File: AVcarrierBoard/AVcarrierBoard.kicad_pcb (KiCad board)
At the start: 4 copper layers, 253.6 x 59 mm, 18 parts, among them J1 Mech_Switch, J2 Mech_Switch, J3 MainRecov, J4 DrogRecov, J5 Staging, J6 Mech_Switch, U2 WiFi Switch, U3 EggtimerQuantum, U4 EggfinderMini/FeatherGPS, U5 Blue_Raven

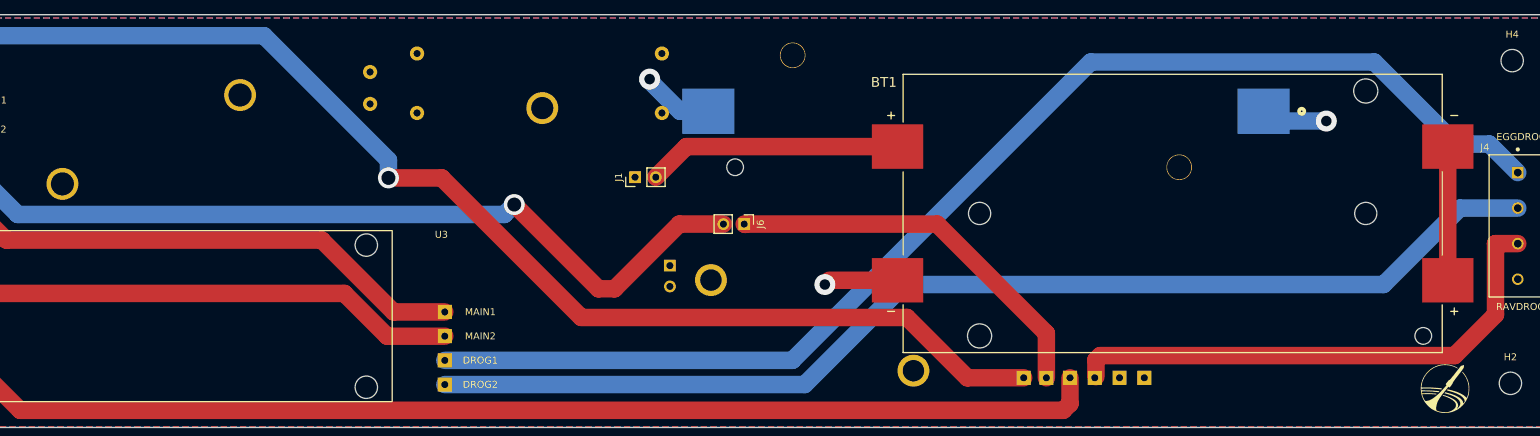
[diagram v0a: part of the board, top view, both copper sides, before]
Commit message: Solved DRC
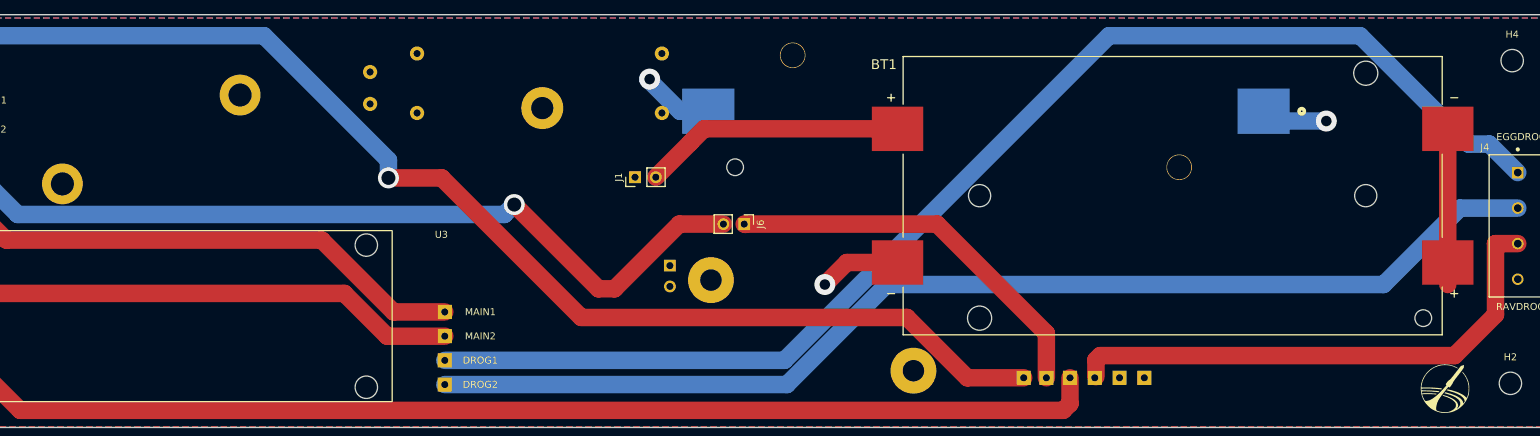
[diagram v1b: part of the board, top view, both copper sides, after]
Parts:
- moved BT1 2.54 mm to (221.3, 91.4)
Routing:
- net DROG1: track 177.6 -> 180.7 mm
- net +7.5V: track 36.4 -> 37.4 mm
- net GND: track 10.6 -> 11.7 mm
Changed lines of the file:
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@@
   )
   (footprint "COTS_Boards:BAT_1048P" (layer "F.Cu")
-    (at 221.32 93.98)
+    (at 221.32 91.44)
     (property "Sheetfile" "AVcarrierBoard.kicad_sch")
     (property "Sheetname" "")
@@
         (effects (font (size 1 1) (thickness 0.15)) (justify mirror))
     )
-    (fp_text user "3rd" (at 51.5 -7.62 -90 unlocked) (layer "B.SilkS")
+    (fp_text user "+" (at 65.5 -7.62 -90 unlocked) (layer "B.SilkS")
+        (effects (font (size 1 1) (thickness 0.15)) (justify mirror))
+    )
+    (fp_text user "Gnd" (at 61.96 -7.62 -90 unlocked) (layer "B.SilkS")
+        (effects (font (size 1 1) (thickness 0.15)) (justify mirror))
+    )
+    (fp_text user "Main" (at 54.88 -7.62 -90 unlocked) (layer "B.SilkS")
+        (effects (font (size 1 1) (thickness 0.15)) (justify mirror))
+    )
+    (fp_text user "4th" (at 48.26 -7.62 270 unlocked) (layer "B.SilkS")
         (effects (font (size 1 1) (thickness 0.15)) (justify mirror))
     )
@@
         (effects (font (size 1 1) (thickness 0.15)) (justify mirror))
     )
-    (fp_text user "4th" (at 48.26 -7.62 270 unlocked) (layer "B.SilkS")
-        (effects (font (size 1 1) (thickness 0.15)) (justify mirror))
-    )
-    (fp_text user "Main" (at 54.88 -7.62 -90 unlocked) (layer "B.SilkS")
-        (effects (font (size 1 1) (thickness 0.15)) (justify mirror))
-    )
-    (fp_text user "Gnd" (at 61.96 -7.62 -90 unlocked) (layer "B.SilkS")
-        (effects (font (size 1 1) (thickness 0.15)) (justify mirror))
-    )
-    (fp_text user "+" (at 65.5 -7.62 -90 unlocked) (layer "B.SilkS")
+    (fp_text user "3rd" (at 51.5 -7.62 -90 unlocked) (layer "B.SilkS")
         (effects (font (size 1 1) (thickness 0.15)) (justify mirror))
     )
@@
     (fp_rect (start 0 2.54) (end 68.58 -22.86)
       (stroke (width 0.05) (type default)) (fill none) (layer "B.CrtYd"))
-    (pad "" np_thru_hole circle (at 3.556 -16.51) (size 4.56 4.56) (drill 3.06832) (layers "F&B.Cu" "*.Mask"))
-    (pad "" np_thru_hole circle (at 32.4993 -3.556) (size 4.56 4.56) (drill 3.06832) (layers "F&B.Cu" "*.Mask"))
+    (pad "" np_thru_hole circle (at 3.556 -16.51) (size 6.56082 6.56082) (drill 3.06832) (layers "*.Cu" "*.Mask"))
+    (pad "" np_thru_hole circle (at 32.4993 -3.556) (size 6.56082 6.56082) (drill 3.06832) (layers "*.Cu" "*.Mask"))
     (pad "1" thru_hole rect (at 65.5 -2.54 90) (size 2.032 2.032) (drill 1) (layers "*.Cu" "*.Mask")
       (net 11 "WIFI_PWR_1S") (pinfunction "+") (pintype "input"))
@@
     (fp_rect (start -2 2) (end 49.08 -22)
       (stroke (width 0.05) (type default)) (fill none) (layer "B.CrtYd"))
-    (pad "" np_thru_hole circle (at 3.302 -3.81) (size 4.56 4.56) (drill 3.302) (layers "F&B.Cu" "*.Mask"))
-    (pad "" np_thru_hole circle (at 28.702 -16.51) (size 4.56 4.56) (drill 3.302) (layers "F&B.Cu" "*.Mask"))
+    (pad "" np_thru_hole circle (at 3.302 -3.81) (size 5.842 5.842) (drill 3.302) (layers "*.Cu" "*.Mask"))
+    (pad "" np_thru_hole circle (at 28.702 -16.51) (size 5.842 5.842) (drill 3.302) (layers "*.Cu" "*.Mask"))
     (pad "1" thru_hole circle (at 47.284587 -15.24) (size 2.032 2.032) (drill 1) (layers "*.Cu" "*.Mask")
       (net 16 "PWR_2S") (pinfunction "VDD") (pintype "power_in"))
@@
         (effects (font (size 1 1) (thickness 0.15)) (justify mirror))
     )
+    (fp_text user "BATT" (at 19.66 5.81 180 unlocked) (layer "B.SilkS")
+        (effects (font (size 1 1) (thickness 0.1)) (justify left bottom mirror))
+    )
     (fp_text user "OUT" (at -6 5 180 unlocked) (layer "B.SilkS")
         (effects (font (size 1 1) (thickness 0.1)) (justify left bottom mirror))
     )
+    (fp_text user "-" (at 23 10.5 180 unlocked) (layer "B.SilkS")
+        (effects (font (size 1 1) (thickness 0.15)) (justify mirror))
+    )
     (fp_text user "+" (at 23 2 180 unlocked) (layer "B.SilkS")
         (effects (font (size 1 1) (thickness 0.15)) (justify mirror))
@@
         (effects (font (size 1 1) (thickness 0.15)) (justify mirror))
     )
-    (fp_text user "-" (at 23 10.5 180 unlocked) (layer "B.SilkS")
-        (effects (font (size 1 1) (thickness 0.15)) (justify mirror))
-    )
     (fp_text user "+" (at -4 2 180 unlocked) (layer "B.SilkS")
         (effects (font (size 1 1) (thickness 0.15)) (justify mirror))
-    )
-    (fp_text user "BATT" (at 19.66 5.81 180 unlocked) (layer "B.SilkS")
-        (effects (font (size 1 1) (thickness 0.1)) (justify left bottom mirror))
     )
     (fp_text user "${REFERENCE}" (at 0 -2.5 180 unlocked) (layer "B.Fab")
@@
     (fp_rect (start 0 38) (end 19 0)
       (stroke (width 0.1) (type default)) (fill none) (layer "B.Fab"))
-    (pad "" np_thru_hole circle (at 9.9 9.8) (size 4.56 4.56) (drill 3.18) (layers "F&B.Cu" "*.Mask"))
+    (pad "" np_thru_hole circle (at 9.9 9.8) (size 6 6) (drill 3.18) (layers "*.Cu" "*.Mask"))
     (pad "1" thru_hole circle (at 27 2) (size 2.032 2.032) (drill 1) (layers "*.Cu" "*.Mask")
       (net 7 "COTSWIFI+") (pinfunction "Batt+") (pintype "power_in"))
@@
   )
   (via (at 243.2812 80.772) (size 3) (drill 1.5) (layers "F.Cu" "B.Cu") (free) (net 1))
+  (segment (start 243.2812 80.772) (end 219.9132 104.14) (width 2.5) (layer "In1.Cu") (net 1))
+  (segment (start 219.9132 104.14) (end 180.34 104.14) (width 2.5) (layer "In1.Cu") (net 1))
+  (segment (start 180.34 104.14) (end 171.958 112.522) (width 2.5) (layer "In1.Cu") (net 1))
+  (segment (start 155.4988 112.522) (end 149.4536 106.4768) (width 2.5) (layer "In1.Cu") (net 1))
   (segment (start 149.4536 106.4768) (end 149.4536 104.4126) (width 2.5) (layer "In1.Cu") (net 1))
-  (segment (start 217.3732 106.68) (end 177.8 106.68) (width 2.5) (layer "In1.Cu") (net 1))
-  (segment (start 243.2812 80.772) (end 217.3732 106.68) (width 2.5) (layer "In1.Cu") (net 1))
   (segment (start 171.958 112.522) (end 155.4988 112.522) (width 2.5) (layer "In1.Cu") (net 1))
-  (segment (start 155.4988 112.522) (end 149.4536 106.4768) (width 2.5) (layer "In1.Cu") (net 1))
-  (segment (start 177.8 106.68) (end 171.958 112.522) (width 2.5) (layer "In1.Cu") (net 1))
   (segment (start 235.712 80.772) (end 234.315 79.375) (width 2.5) (layer "B.Cu") (net 1))
   (segment (start 243.2812 80.772) (end 235.712 80.772) (width 2.5) (layer "B.Cu") (net 1))
-  (segment (start 181.99 103.535) (end 172.2074 103.535) (width 2.5) (layer "F.Cu") (net 2))
+  (segment (start 174.7474 100.995) (end 181.99 100.995) (width 2.5) (layer "F.Cu") (net 2))
+  (segment (start 172.2074 103.535) (end 174.7474 100.995) (width 2.5) (layer "F.Cu") (net 2))
   (segment (start 172.2074 103.535) (end 171.6024 104.14) (width 0.25) (layer "F.Cu") (net 2))
   (via (at 171.6024 104.14) (size 3) (drill 1.5) (layers "F.Cu" "B.Cu") (net 2))
@@
   (segment (start 155.3972 78.2072) (end 155.3972 90.5256) (width 2.5) (layer "In1.Cu") (net 7))
   (segment (start 149.4536 96.4692) (end 149.4536 101.4426) (width 2.5) (layer "In1.Cu") (net 7))
-  (segment (start 151.8136 84.425) (end 181.99 84.425) (width 2.5) (layer "F.Cu") (net 8))
-  (segment (start 147.4402 88.7984) (end 151.8136 84.425) (width 2.5) (layer "F.Cu") (net 8))
+  (segment (start 147.4402 88.7984) (end 152.4 83.8386) (width 2.5) (layer "F.Cu") (net 8))
+  (segment (start 152.4 83.82) (end 154.335 81.885) (width 2.5) (layer "F.Cu") (net 8))
+  (segment (start 152.4 83.8386) (end 152.4 83.82) (width 2.5) (layer "F.Cu") (net 8))
+  (segment (start 154.335 81.885) (end 181.99 81.885) (width 2.5) (layer "F.Cu") (net 8))
+  (segment (start 248.125839 68.58) (end 212.217151 68.58) (width 2.5) (layer "B.Cu") (net 9))
   (segment (start 270.65 88.1375) (end 266.576 84.0635) (width 2.5) (layer "B.Cu") (net 9))
-  (segment (start 166.96 114.98) (end 117.275 114.98) (width 2.5) (layer "B.Cu") (net 9))
-  (segment (start 250.1392 72.3392) (end 209.6008 72.3392) (width 2.5) (layer "B.Cu") (net 9))
-  (segment (start 266.576 84.0635) (end 261.8635 84.0635) (width 2.5) (layer "B.Cu") (net 9))
-  (segment (start 209.6008 72.3392) (end 166.96 114.98) (width 2.5) (layer "B.Cu") (net 9))
-  (segment (start 261.8635 84.0635) (end 250.1392 72.3392) (width 2.5) (layer "B.Cu") (net 9))
-  (segment (start 183.015527 104.14) (end 168.715527 118.44) (width 2.5) (layer "B.Cu") (net 10))
+  (segment (start 165.817151 114.98) (end 117.275 114.98) (width 2.5) (layer "B.Cu") (net 9))
+  (segment (start 266.576 84.0635) (end 263.609339 84.0635) (width 2.5) (layer "B.Cu") (net 9))
+  (segment (start 263.609339 84.0635) (end 248.125839 68.58) (width 2.5) (layer "B.Cu") (net 9))
+  (segment (start 212.217151 68.58) (end 165.817151 114.98) (width 2.5) (layer "B.Cu") (net 9))
+  (segment (start 166.175527 118.44) (end 117.275 118.44) (width 2.5) (layer "B.Cu") (net 10))
+  (segment (start 180.475527 104.14) (end 166.175527 118.44) (width 2.5) (layer "B.Cu") (net 10))
   (segment (start 262.3825 93.2175) (end 251.46 104.14) (width 2.5) (layer "B.Cu") (net 10))
-  (segment (start 251.46 104.14) (end 183.015527 104.14) (width 2.5) (layer "B.Cu") (net 10))
-  (segment (start 168.715527 118.44) (end 117.275 118.44) (width 2.5) (layer "B.Cu") (net 10))
   (segment (start 270.65 93.2175) (end 262.3825 93.2175) (width 2.5) (layer "B.Cu") (net 10))
+  (segment (start 251.46 104.14) (end 180.475527 104.14) (width 2.5) (layer "B.Cu") (net 10))
   (segment (start 160.2308 95.504) (end 160.2308 95.5548) (width 2.5) (layer "F.Cu") (net 12))
   (segment (start 187.647386 95.504) (end 160.0708 95.504) (width 2.5) (layer "F.Cu") (net 12))

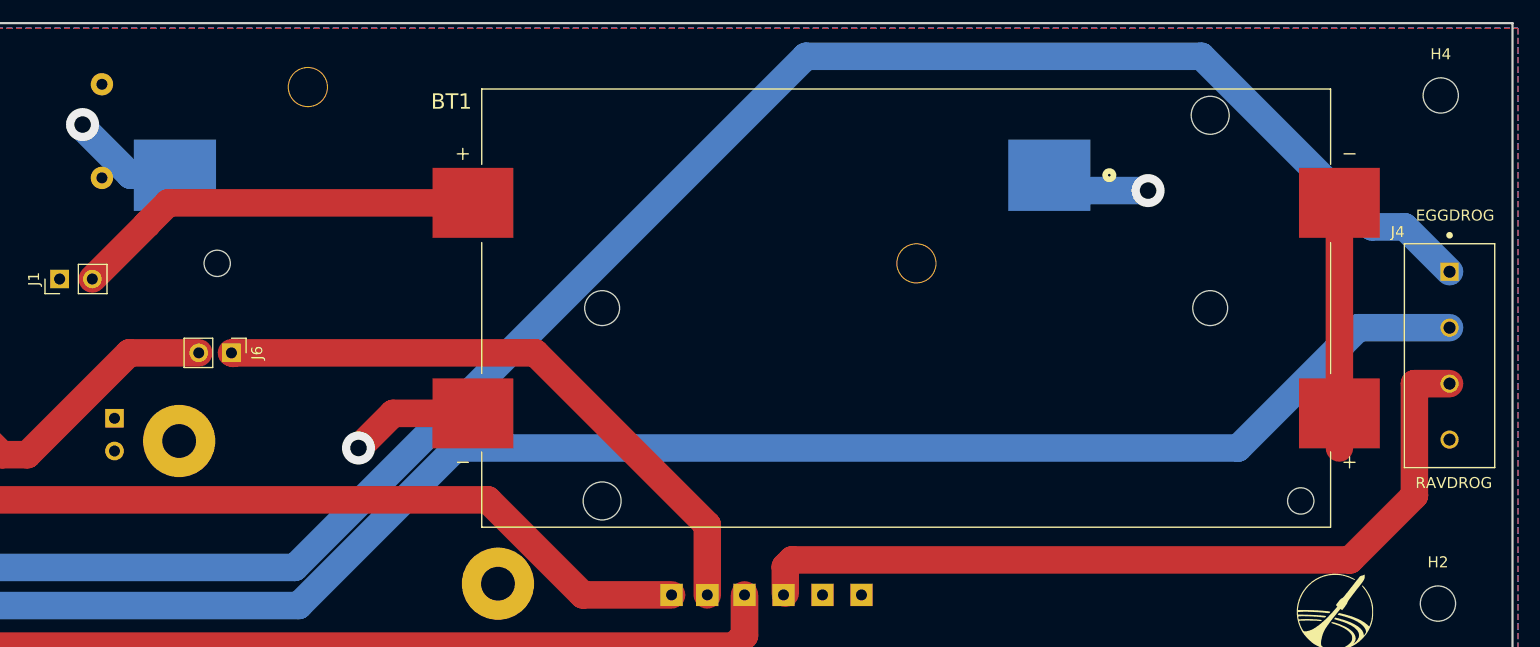
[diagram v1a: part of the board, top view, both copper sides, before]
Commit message: Changed location of 1S battery and remade STEP
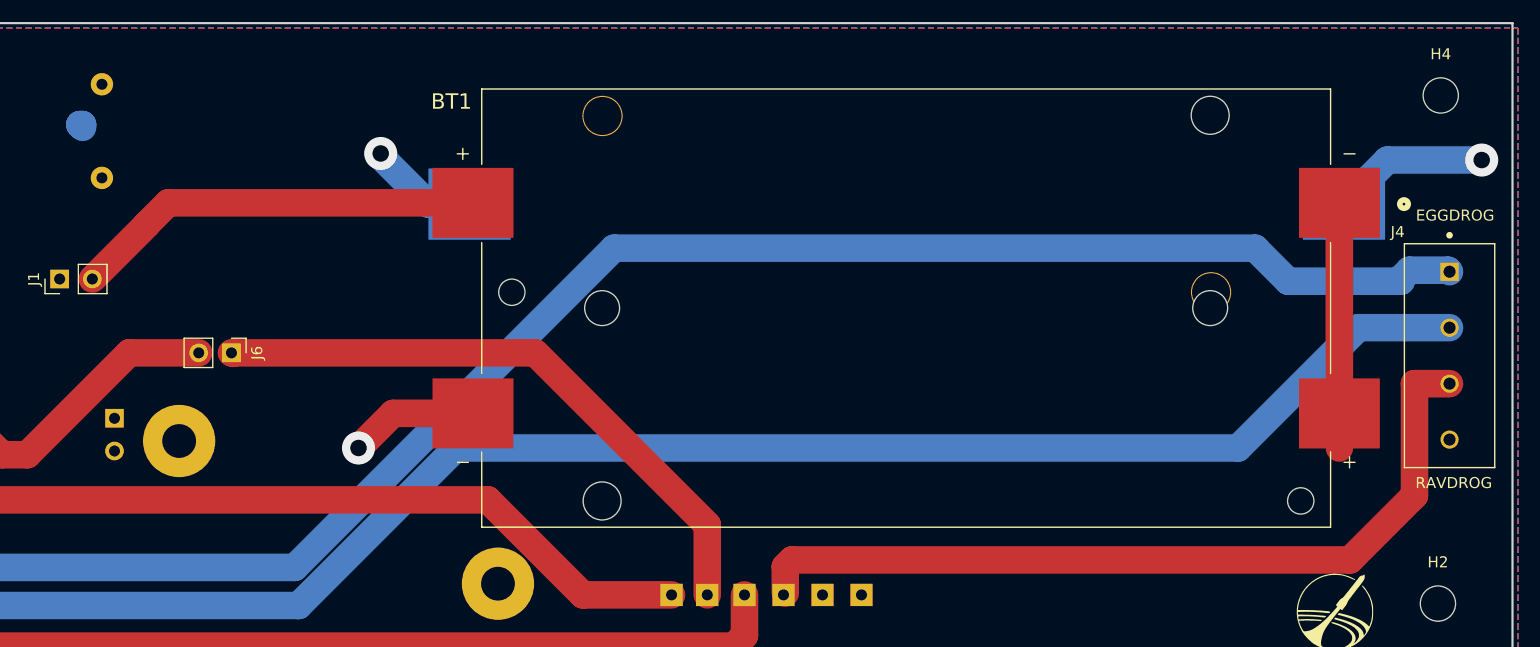
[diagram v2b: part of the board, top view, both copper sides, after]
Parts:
- moved BT2 26.9 mm to (221.4, 82.0)
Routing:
- net +3V8: track 121.1 -> 157.2 mm
- net DROG1: track 180.7 -> 167.2 mm
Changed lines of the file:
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@@
   )
   (footprint "COTS_Boards:1042P_KEY" (layer "B.Cu")
-    (at 194.6275 79.375 180)
+    (at 221.3775 81.999 180)
     (tags "1042P ")
     (property "Sheetfile" "AVcarrierBoard.kicad_sch")
@@
     (effects (font (size 1 1) (thickness 0.15)) (justify right bottom))
   )
-  (via (at 243.2812 80.772) (size 3) (drill 1.5) (layers "F.Cu" "B.Cu") (free) (net 1))
+  (via (at 273.5692 78) (size 3) (drill 1.5) (layers "F.Cu" "B.Cu") (free) (net 1))
+  (segment (start 251.228 80.772) (end 254 78) (width 2.5) (layer "In1.Cu") (net 1))
   (segment (start 243.2812 80.772) (end 219.9132 104.14) (width 2.5) (layer "In1.Cu") (net 1))
+  (segment (start 254 78) (end 273.5692 78) (width 2.5) (layer "In1.Cu") (net 1))
+  (segment (start 243.2812 80.772) (end 251.228 80.772) (width 2.5) (layer "In1.Cu") (net 1))
   (segment (start 219.9132 104.14) (end 180.34 104.14) (width 2.5) (layer "In1.Cu") (net 1))
   (segment (start 180.34 104.14) (end 171.958 112.522) (width 2.5) (layer "In1.Cu") (net 1))
@@
   (segment (start 149.4536 106.4768) (end 149.4536 104.4126) (width 2.5) (layer "In1.Cu") (net 1))
   (segment (start 171.958 112.522) (end 155.4988 112.522) (width 2.5) (layer "In1.Cu") (net 1))
-  (segment (start 235.712 80.772) (end 234.315 79.375) (width 2.5) (layer "B.Cu") (net 1))
-  (segment (start 243.2812 80.772) (end 235.712 80.772) (width 2.5) (layer "B.Cu") (net 1))
+  (segment (start 265 78) (end 273.5692 78) (width 2.5) (layer "B.Cu") (net 1))
+  (segment (start 261.065 81.999) (end 261.065 81.935) (width 0.25) (layer "B.Cu") (net 1))
+  (segment (start 273.5682 78) (end 273.5692 78.001) (width 2.5) (layer "B.Cu") (net 1))
+  (segment (start 261.065 81.935) (end 265 78) (width 2.5) (layer "B.Cu") (net 1))
   (segment (start 174.7474 100.995) (end 181.99 100.995) (width 2.5) (layer "F.Cu") (net 2))
   (segment (start 172.2074 103.535) (end 174.7474 100.995) (width 2.5) (layer "F.Cu") (net 2))
@@
   (segment (start 152.4 83.8386) (end 152.4 83.82) (width 2.5) (layer "F.Cu") (net 8))
   (segment (start 154.335 81.885) (end 181.99 81.885) (width 2.5) (layer "F.Cu") (net 8))
-  (segment (start 248.125839 68.58) (end 212.217151 68.58) (width 2.5) (layer "B.Cu") (net 9))
-  (segment (start 270.65 88.1375) (end 266.576 84.0635) (width 2.5) (layer "B.Cu") (net 9))
+  (segment (start 270.5125 88) (end 267 88) (width 2.5) (layer "B.Cu") (net 9))
+  (segment (start 194.797151 86) (end 165.817151 114.98) (width 2.5) (layer "B.Cu") (net 9))
+  (segment (start 267 88) (end 266.2488 88.7512) (width 2.5) (layer "B.Cu") (net 9))
+  (segment (start 270.65 88.1375) (end 270.5125 88) (width 2.5) (layer "B.Cu") (net 9))
+  (segment (start 266.2488 88.7512) (end 266.2488 89) (width 2.5) (layer "B.Cu") (net 9))
   (segment (start 165.817151 114.98) (end 117.275 114.98) (width 2.5) (layer "B.Cu") (net 9))
-  (segment (start 266.576 84.0635) (end 263.609339 84.0635) (width 2.5) (layer "B.Cu") (net 9))
-  (segment (start 263.609339 84.0635) (end 248.125839 68.58) (width 2.5) (layer "B.Cu") (net 9))
-  (segment (start 212.217151 68.58) (end 165.817151 114.98) (width 2.5) (layer "B.Cu") (net 9))
+  (segment (start 266.2488 89) (end 256 89) (width 2.5) (layer "B.Cu") (net 9))
+  (segment (start 256 89) (end 253 86) (width 2.5) (layer "B.Cu") (net 9))
+  (segment (start 253 86) (end 194.797151 86) (width 2.5) (layer "B.Cu") (net 9))
   (segment (start 166.175527 118.44) (end 117.275 118.44) (width 2.5) (layer "B.Cu") (net 10))
   (segment (start 180.475527 104.14) (end 166.175527 118.44) (width 2.5) (layer "B.Cu") (net 10))
@@
   (segment (start 267.4625 98.2975) (end 267.4625 108.4575) (width 2.5) (layer "F.Cu") (net 13))
   (segment (start 270.65 98.2975) (end 267.4625 98.2975) (width 2.5) (layer "F.Cu") (net 13))
-  (via (at 146.558 74.7776) (size 3) (drill 1.5) (layers "F.Cu" "B.Cu") (net 14))
+  (via (at 173.618 77.4026) (size 3) (drill 1.5) (layers "F.Cu" "B.Cu") (net 14))
   (segment (start 146.558 74.7776) (end 146.304 74.7776) (width 2.5) (layer "B.Cu") (net 14))
-  (segment (start 154.94 79.375) (end 150.9014 79.375) (width 2.5) (layer "B.Cu") (net 14))
-  (segment (start 150.9014 79.375) (end 146.558 75.0316) (width 2.5) (layer "B.Cu") (net 14))
+  (segment (start 182 82) (end 177.9614 82) (width 2.5) (layer "B.Cu") (net 14))
+  (segment (start 177.9614 82) (end 173.618 77.6566) (width 2.5) (layer "B.Cu") (net 14))
   (segment (start 146.558 75.0316) (end 146.558 74.7776) (width 2.5) (layer "B.Cu") (net 14))
   (segment (start 146.304 74.7776) (end 146.4564 74.93) (width 2.5) (layer "B.Cu") (net 14))
